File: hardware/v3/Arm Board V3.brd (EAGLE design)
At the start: 165.1 x 76.2 mm, 49 parts, among them CN1 1X4-BIG, IC1 L6208D, IC2 L6208D, IC3 L6208D, Q3 Q_LTC490, U1 MAX3468CSA

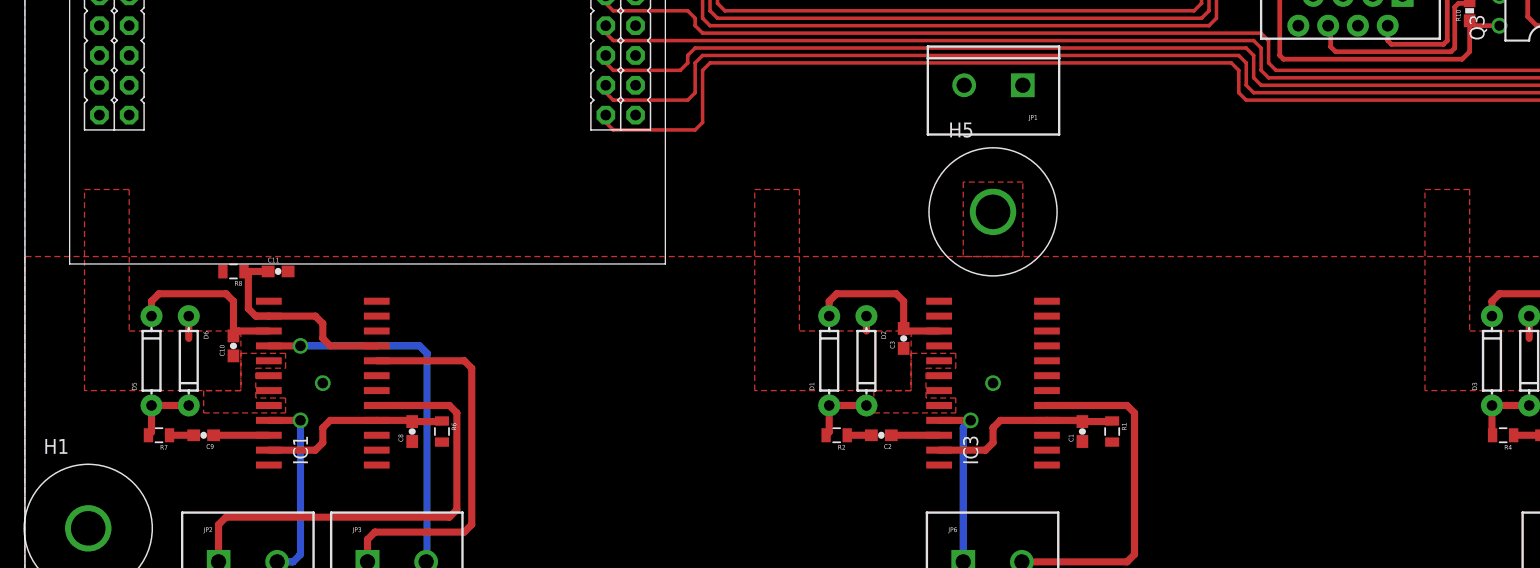
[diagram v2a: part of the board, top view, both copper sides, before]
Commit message: Did some more routing on the board
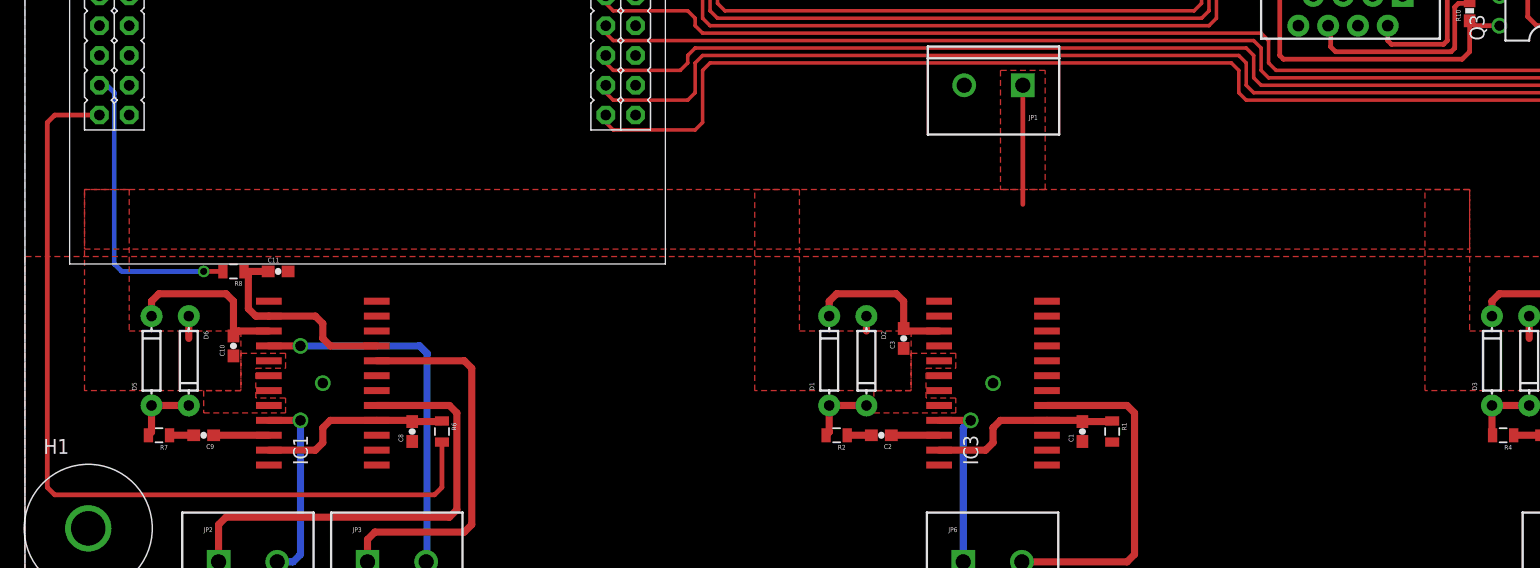
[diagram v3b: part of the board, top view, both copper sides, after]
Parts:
- removed H5: (no value), Lib_TH:H_MNTHOLE_#4
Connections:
- removed net VS: C10.1, C3.1, C6.1, D2.A, D4.A, D6.A, IC1.17, IC1.20, IC2.17, IC2.20, IC3.17, IC3.20
- net GND: no longer H5.1
- net VIN: now also C10.1, C3.1, C6.1, D2.A, D4.A, D6.A, IC1.17, IC1.20, IC2.17, IC2.20, IC3.17, IC3.20
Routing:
- net EN_A_1: track 0.00 -> 73.9 mm
- net EN_B_1: track 0.00 -> 25.7 mm, vias 0 -> 1
- net VIN: track 0.00 -> 15.2 mm
- net VS: track 5.08 -> 0.00 mm
- added copper zone on layer 1, net VIN
- removed copper zone on layer 1, net VS
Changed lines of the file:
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@@
 <element name="H3" library="Lib_TH" package="H_MNTHOLE_#4" value="" x="159.7025" y="70.8025"/>
 <element name="H4" library="Lib_TH" package="H_MNTHOLE_#4" value="" x="159.7025" y="5.3975"/>
-<element name="H5" library="Lib_TH" package="H_MNTHOLE_#4" value="" x="82.55" y="32.385"/>
 </elements>
 <signals>
@@
 <contactref element="H4" pad="1"/>
 <via x="25.4" y="17.78" extent="1-16" drill="0.9" shape="octagon"/>
-<contactref element="H5" pad="1"/>
-<polygon width="0.4064" layer="1">
-<vertex x="80.01" y="34.925"/>
-<vertex x="80.01" y="28.575"/>
-<vertex x="85.09" y="28.575"/>
-<vertex x="85.09" y="34.925"/>
-</polygon>
 <via x="82.55" y="17.78" extent="1-16" drill="0.9" shape="octagon"/>
 <via x="139.7" y="17.78" extent="1-16" drill="0.9" shape="octagon"/>
 <wire x1="30" y1="22.225" x2="30" y2="18.415" width="0" layer="19" extent="1-1"/>
+<wire x1="30" y1="13.335" x2="30" y2="17.145" width="0" layer="19" extent="1-1"/>
 </signal>
 <signal name="A1_1">
@@
 <signal name="VIN">
 <contactref element="JP1" pad="1"/>
+<contactref element="C6" pad="1"/>
+<contactref element="D4" pad="A"/>
+<contactref element="IC2" pad="17"/>
+<contactref element="IC2" pad="20"/>
+<wire x1="128.27" y1="23.495" x2="128.27" y2="21.59" width="0.6096" layer="1"/>
+<contactref element="C10" pad="1"/>
+<contactref element="D6" pad="A"/>
+<contactref element="IC1" pad="20"/>
+<contactref element="IC1" pad="17"/>
+<wire x1="13.97" y1="23.495" x2="13.97" y2="21.59" width="0.6096" layer="1"/>
+<contactref element="C3" pad="1"/>
+<contactref element="D2" pad="A"/>
+<contactref element="IC3" pad="17"/>
+<contactref element="IC3" pad="20"/>
+<polygon width="0.254" layer="1">
+<vertex x="18.415" y="22.225"/>
+<vertex x="18.415" y="17.145"/>
+<vertex x="5.08" y="17.145"/>
+<vertex x="5.08" y="34.29"/>
+<vertex x="8.89" y="34.29"/>
+<vertex x="8.89" y="22.225"/>
+</polygon>
+<polygon width="0.254" layer="1" thermals="no">
+<vertex x="15.24" y="17.145"/>
+<vertex x="15.24" y="15.24"/>
+<vertex x="22.225" y="15.24"/>
+<vertex x="22.225" y="16.51"/>
+<vertex x="19.685" y="16.51"/>
+<vertex x="19.685" y="19.05"/>
+<vertex x="22.225" y="19.05"/>
+<vertex x="22.225" y="20.32"/>
+<vertex x="18.415" y="20.32"/>
+<vertex x="18.415" y="17.145"/>
+</polygon>
+<polygon width="0.254" layer="1" thermals="no">
+<vertex x="72.39" y="17.145"/>
+<vertex x="72.39" y="15.24"/>
+<vertex x="79.375" y="15.24"/>
+<vertex x="79.375" y="16.51"/>
+<vertex x="76.835" y="16.51"/>
+<vertex x="76.835" y="19.05"/>
+<vertex x="79.375" y="19.05"/>
+<vertex x="79.375" y="20.32"/>
+<vertex x="75.565" y="20.32"/>
+<vertex x="75.565" y="17.145"/>
+</polygon>
+<polygon width="0.254" layer="1">
+<vertex x="75.565" y="22.225"/>
+<vertex x="75.565" y="17.145"/>
+<vertex x="62.23" y="17.145"/>
+<vertex x="62.23" y="34.29"/>
+<vertex x="66.04" y="34.29"/>
+<vertex x="66.04" y="22.225"/>
+</polygon>
+<wire x1="71.755" y1="23.495" x2="71.755" y2="22.225" width="0.6096" layer="1"/>
+<polygon width="0.254" layer="1" thermals="no">
+<vertex x="129.54" y="17.145"/>
+<vertex x="129.54" y="15.24"/>
+<vertex x="136.525" y="15.24"/>
+<vertex x="136.525" y="16.51"/>
+<vertex x="133.985" y="16.51"/>
+<vertex x="133.985" y="19.05"/>
+<vertex x="136.525" y="19.05"/>
+<vertex x="136.525" y="20.32"/>
+<vertex x="132.715" y="20.32"/>
+<vertex x="132.715" y="17.145"/>
+</polygon>
+<polygon width="0.254" layer="1">
+<vertex x="132.715" y="22.225"/>
+<vertex x="132.715" y="17.145"/>
+<vertex x="119.38" y="17.145"/>
+<vertex x="119.38" y="34.29"/>
+<vertex x="123.19" y="34.29"/>
+<vertex x="123.19" y="22.225"/>
+</polygon>
+<polygon width="0.4064" layer="1">
+<vertex x="5.08" y="34.29"/>
+<vertex x="5.08" y="29.21"/>
+<vertex x="123.19" y="29.21"/>
+<vertex x="123.19" y="34.29"/>
+</polygon>
+<polygon width="0.4064" layer="1" thermals="no">
+<vertex x="83.185" y="44.45"/>
+<vertex x="83.185" y="34.29"/>
+<vertex x="86.995" y="34.29"/>
+<vertex x="86.995" y="44.45"/>
+</polygon>
+<wire x1="85.09" y1="43.18" x2="85.09" y2="33.02" width="0.4064" layer="1"/>
 </signal>
 <signal name="A1_3">
@@
 <contactref element="R6" pad="2"/>
 <contactref element="U$1" pad="PA7"/>
-<wire x1="6.35" y1="40.64" x2="35.56" y2="12.7525" width="0" layer="19" extent="1-1"/>
+<wire x1="35.56" y1="12.7525" x2="35.56" y2="8.89" width="0.4064" layer="1"/>
+<wire x1="35.56" y1="8.89" x2="34.925" y2="8.255" width="0.4064" layer="1"/>
+<wire x1="34.925" y1="8.255" x2="2.54" y2="8.255" width="0.4064" layer="1"/>
+<wire x1="2.54" y1="8.255" x2="1.905" y2="8.89" width="0.4064" layer="1"/>
+<wire x1="1.905" y1="8.89" x2="1.905" y2="40.005" width="0.4064" layer="1"/>
+<wire x1="1.905" y1="40.005" x2="2.54" y2="40.64" width="0.4064" layer="1"/>
+<wire x1="2.54" y1="40.64" x2="6.35" y2="40.64" width="0.4064" layer="1"/>
 </signal>
 <signal name="EN_B_2">
@@
 <contactref element="U$1" pad="PE2"/>
 <wire x1="8.89" y1="45.72" x2="131.18" y2="27.305" width="0" layer="19" extent="1-1"/>
-</signal>
-<signal name="VS">
-<contactref element="C10" pad="1"/>
-<contactref element="D6" pad="A"/>
-<contactref element="IC1" pad="20"/>
-<contactref element="IC1" pad="17"/>
-<contactref element="C6" pad="1"/>
-<contactref element="D4" pad="A"/>
-<contactref element="IC2" pad="17"/>
-<contactref element="IC2" pad="20"/>
-<contactref element="C3" pad="1"/>
-<contactref element="D2" pad="A"/>
-<contactref element="IC3" pad="17"/>
-<contactref element="IC3" pad="20"/>
-<polygon width="0.254" layer="1">
-<vertex x="18.415" y="22.225"/>
-<vertex x="18.415" y="17.145"/>
-<vertex x="5.08" y="17.145"/>
-<vertex x="5.08" y="34.29"/>
-<vertex x="8.89" y="34.29"/>
-<vertex x="8.89" y="22.225"/>
-</polygon>
-<polygon width="0.254" layer="1" thermals="no">
-<vertex x="15.24" y="17.145"/>
-<vertex x="15.24" y="15.24"/>
-<vertex x="22.225" y="15.24"/>
-<vertex x="22.225" y="16.51"/>
-<vertex x="19.685" y="16.51"/>
-<vertex x="19.685" y="19.05"/>
-<vertex x="22.225" y="19.05"/>
-<vertex x="22.225" y="20.32"/>
-<vertex x="18.415" y="20.32"/>
-<vertex x="18.415" y="17.145"/>
-</polygon>
-<polygon width="0.254" layer="1" thermals="no">
-<vertex x="72.39" y="17.145"/>
-<vertex x="72.39" y="15.24"/>
-<vertex x="79.375" y="15.24"/>
-<vertex x="79.375" y="16.51"/>
-<vertex x="76.835" y="16.51"/>
-<vertex x="76.835" y="19.05"/>
-<vertex x="79.375" y="19.05"/>
-<vertex x="79.375" y="20.32"/>
-<vertex x="75.565" y="20.32"/>
-<vertex x="75.565" y="17.145"/>
-</polygon>
-<polygon width="0.254" layer="1">
-<vertex x="75.565" y="22.225"/>
-<vertex x="75.565" y="17.145"/>
-<vertex x="62.23" y="17.145"/>
-<vertex x="62.23" y="34.29"/>
-<vertex x="66.04" y="34.29"/>
-<vertex x="66.04" y="22.225"/>
-</polygon>
-<wire x1="71.755" y1="23.495" x2="71.755" y2="22.225" width="0.6096" layer="1"/>
-<wire x1="13.97" y1="23.495" x2="13.97" y2="21.59" width="0.6096" layer="1"/>
-<polygon width="0.254" layer="1" thermals="no">
-<vertex x="129.54" y="17.145"/>
-<vertex x="129.54" y="15.24"/>
-<vertex x="136.525" y="15.24"/>
-<vertex x="136.525" y="16.51"/>
-<vertex x="133.985" y="16.51"/>
-<vertex x="133.985" y="19.05"/>
-<vertex x="136.525" y="19.05"/>
-<vertex x="136.525" y="20.32"/>
-<vertex x="132.715" y="20.32"/>
-<vertex x="132.715" y="17.145"/>
-</polygon>
-<polygon width="0.254" layer="1">
-<vertex x="132.715" y="22.225"/>
-<vertex x="132.715" y="17.145"/>
-<vertex x="119.38" y="17.145"/>
-<vertex x="119.38" y="34.29"/>
-<vertex x="123.19" y="34.29"/>
-<vertex x="123.19" y="22.225"/>
-</polygon>
-<wire x1="128.27" y1="23.495" x2="128.27" y2="21.59" width="0.6096" layer="1"/>
-<wire x1="77.95" y1="19.685" x2="128.27" y2="21.59" width="0" layer="19" extent="1-1"/>
-<wire x1="20.8" y1="19.685" x2="71.755" y2="22.225" width="0" layer="19" extent="1-1"/>
 </signal>
 <signal name="N$9">
@@
 <contactref element="R8" pad="2"/>
 <contactref element="U$1" pad="PA6"/>
-<wire x1="16.88" y1="27.305" x2="6.35" y2="43.18" width="0" layer="19" extent="1-1"/>
+<wire x1="16.88" y1="27.305" x2="15.24" y2="27.305" width="0.4064" layer="1"/>
+<via x="15.24" y="27.305" extent="1-16" drill="0.6" shape="octagon"/>
+<wire x1="15.24" y1="27.305" x2="8.255" y2="27.305" width="0.4064" layer="16"/>
+<wire x1="8.255" y1="27.305" x2="7.62" y2="27.94" width="0.4064" layer="16"/>
+<wire x1="7.62" y1="27.94" x2="7.62" y2="42.545" width="0.4064" layer="16"/>
+<wire x1="7.62" y1="42.545" x2="6.985" y2="43.18" width="0.4064" layer="16"/>
+<wire x1="6.985" y1="43.18" x2="6.35" y2="43.18" width="0.4064" layer="16"/>
 </signal>
 <signal name="RESET">

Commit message: Moved a few things around
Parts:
- moved JP1 6.35 mm to (85.1, 36.8)
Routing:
- net VIN: track 15.2 -> 12.7 mm
- net EN485: track 90.2 -> 92.2 mm
- net RXD2: track 84.3 -> 85.6 mm
- net XRESET: track 116.2 -> 115.0 mm
- net TXD3: track 109.8 -> 108.5 mm
- net TXD2: track 86.8 -> 88.0 mm
- net RXD3: track 103.9 -> 102.7 mm

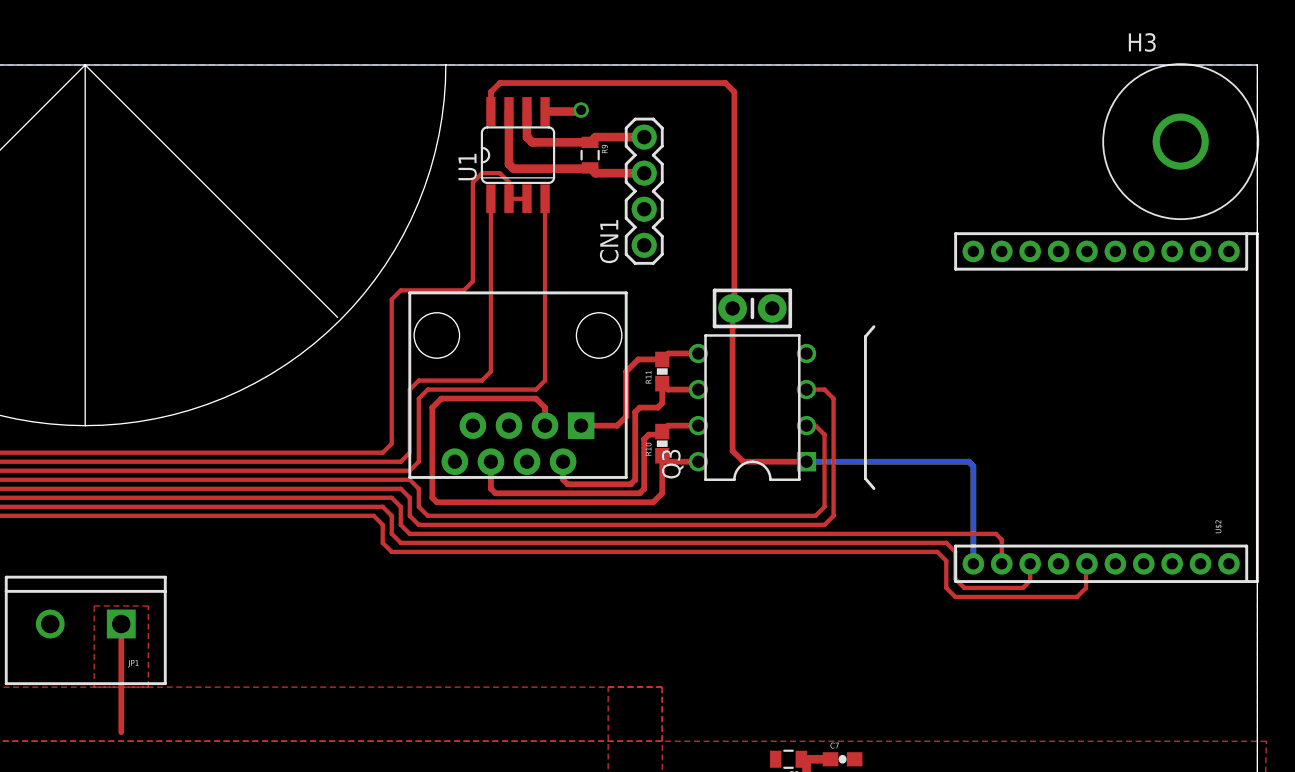
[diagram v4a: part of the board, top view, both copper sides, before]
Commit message: Redid Xbee as well as moved things around
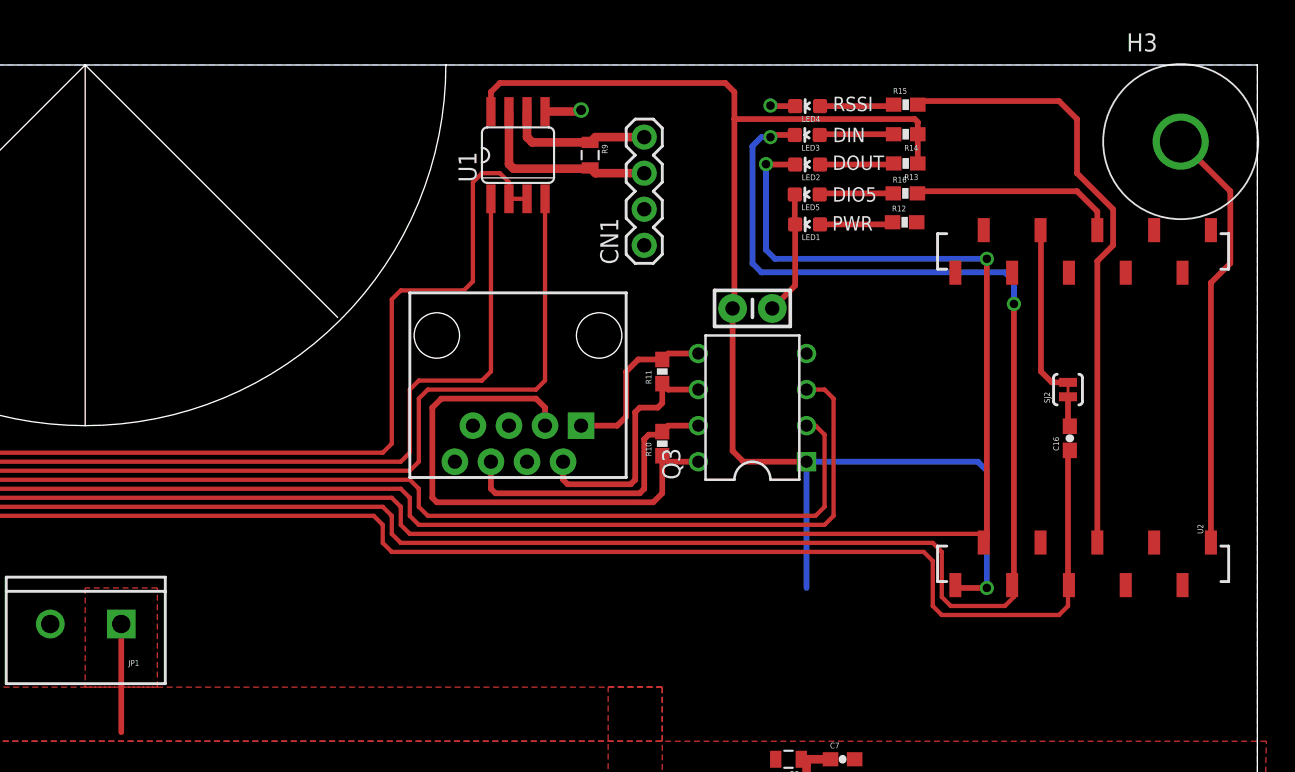
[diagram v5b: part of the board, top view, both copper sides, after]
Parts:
- removed U$2: XBEE-1B2, SparkFun-RF:XBEE-SILK
- added C16: 0.1uF, SparkFun-Capacitors:0603-CAP
- added LED1, LED2: Red, SparkFun-LED:LED-0603
- added LED3, LED4, LED5: Green, SparkFun-LED:LED-0603
- added R12, R13, R14, R15, R16: 1k, SparkFun-Resistors:0603-RES
- added SJ2: SOLDERJUMPERTRACE, SparkFun:SJ_2S-TRACE
- added U2: XBEE-1B3, SparkFun:XBEE-SMD
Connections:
- new net CTS: U2.12
- new net DIO0: U2.20
- new net DIO1: U2.19
- new net DIO11: U2.7
- new net DIO12: U2.4
- new net DIO2: U2.18
- new net DIO3: SJ2.2, U2.17
- new net DIO4: U2.11
- new net DIO5: R16.2, U2.15
- new net DIO9: U2.13
- new net DTR: U2.9
- new net N$11: C16.2, SJ2.1
- new net N$139: LED5.A, R16.1
- new net N$38: LED1.A, R12.1
- new net N$4: LED2.A, R13.2
- new net N$6: LED3.A, R14.2
- new net N$7: LED4.A, R15.1
- new net RES1: U2.8
- new net RES2: U2.14
- new net RSSI: R15.2, U2.6
- new net RTS: U2.16
- net +3V3: now also R12.2, R13.1, R14.1, U2.1; no longer U$2.1
- net GND: now also LED1.C, LED4.C, LED5.C, U2.10; no longer U$2.10
- net RXD3: now also LED2.C, U2.2; no longer U$2.2
- net TXD3: now also LED3.C, U2.3; no longer U$2.3
- net XRESET: now also C16.1, U2.5; no longer U$2.5
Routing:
- net TXD3: track 108.5 -> 160.3 mm, vias 0 -> 2
- net RSSI: track 0.00 -> 43.2 mm
- net RXD3: track 102.7 -> 143.7 mm, vias 0 -> 2
- net GND: track 2.58 -> 43.6 mm, vias 4 -> 5
- net +3V3: track 68.6 -> 98.2 mm, vias 0 -> 1
- net DIO5: track 0.00 -> 14.6 mm
- net DIO3: track 0.00 -> 12.2 mm
- net XRESET: track 115.0 -> 124.3 mm
- net N$6: track 0.00 -> 5.23 mm
- net N$7: track 0.00 -> 5.22 mm
- net N$4: track 0.00 -> 5.21 mm
- net N$139: track 0.00 -> 5.21 mm
- net N$38: track 0.00 -> 5.17 mm
- net N$11: track 0.00 -> 2.12 mm
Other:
- board text added: "DIN"
- board text added: "DIO5"
- board text added: "DOUT"
- board text added: "PWR"
- board text added: "RSSI"

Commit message: Changed some stuff on launchpad
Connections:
- net VBUS renamed +5V
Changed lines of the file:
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@@
 <wire x1="105.41" y1="43.18" x2="146.05" y2="43.18" width="0.3048" layer="1"/>
-</signal>
-<signal name="VBUS">
-<contactref element="U$1" pad="VBUS"/>
 </signal>
 <signal name="+3V3">
@@
 <wire x1="134.354" y1="67.1576" x2="134.2778" y2="67.0814" width="0.4064" layer="1"/>
 </signal>
+<signal name="+5V">
+<contactref element="U$1" pad="VBUS"/>
+</signal>
 </signals>

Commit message: Routed stuffs and stuffs and moved stuff and stuffs
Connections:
- net EN_A_1: now also U$1.PE1; no longer U$1.PA7
- net EN_A_2: now also U$1.PB7; no longer U$1.PE3
- net EN_A_3: no longer U$1.PA5
- net EN_B_1: now also U$1.PE2; no longer U$1.PA6
- net EN_B_2: now also U$1.PB6; no longer U$1.PE2
- net IN1_A_1: now also U$1.PD1
- net IN1_A_2: now also U$1.PA4
- net IN1_B_1: now also U$1.PD2
- net IN1_B_2: now also U$1.PA2
- net IN2_A_1: now also U$1.PD0
- net IN2_A_2: now also U$1.PA3
- net IN2_B_1: now also U$1.PD3
- net IN2_B_2: now also U$1.PE0
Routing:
- net IN2_A_1: track 0.00 -> 86.7 mm
- net IN1_A_1: track 0.00 -> 76.7 mm
- net IN1_B_1: track 0.00 -> 54.2 mm, vias 0 -> 1
- net IN1_A_2: track 0.00 -> 50.7 mm, vias 0 -> 1
- net IN2_B_1: track 0.00 -> 45.9 mm, vias 0 -> 1
- net IN2_A_2: track 0.00 -> 45.4 mm, vias 0 -> 1
- net EN_A_2: track 0.00 -> 37.1 mm, vias 0 -> 1
- net IN1_B_2: track 0.00 -> 26.7 mm
- net IN2_B_2: track 0.00 -> 13.0 mm
- net EN_B_2: track 0.00 -> 10.6 mm
- net EN_A_1: track 73.9 -> 83.3 mm, vias 0 -> 1
- net EN_B_1: track 25.7 -> 28.2 mm
